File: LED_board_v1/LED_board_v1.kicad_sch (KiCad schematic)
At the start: 0 parts

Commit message: テープLED基板を作った(要修正+シルクメモ追加)
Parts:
- added C1, C13, C14, C15, C16, C19, C21, C4, C6, C8: 0.1uF, Capacitor_SMD:C_0603_1608Metric_Pad1.08x0.95mm_HandSolder, symbol Device:C_Small
- added C10, C12, C20, C9: 4.7μF, Capacitor_SMD:C_0805_2012Metric_Pad1.18x1.45mm_HandSolder, symbol Device:C
- added C11: 22μF, Capacitor_SMD:C_0805_2012Metric_Pad1.18x1.45mm_HandSolder, symbol Device:C
- added C17, C18: 4.7uF, Capacitor_SMD:C_0603_1608Metric_Pad1.08x0.95mm_HandSolder, symbol Device:C_Small
- added C5, C7: 100uF, Capacitor_THT:CP_Radial_D8.0mm_P3.50mm, symbol Device:C_Polarized
- added D2: D_Shockley, Diode_SMD:D_SOD-323_HandSoldering, symbol Device:D_Shockley
- added FB1: 120, Inductor_SMD:L_0603_1608Metric_Pad1.05x0.95mm_HandSolder, symbol Device:FerriteBead_Small
- added J1, J3: Conn_01x03_Pin, Connector_JST:JST_XH_S3B-XH-A_1x03_P2.50mm_Horizontal, symbol Connector:Conn_01x03_Pin
- added J12: Conn_01x02_Pin, Connector_AMASS:AMASS_XT30PW-M_1x02_P2.50mm_Horizontal, symbol Connector:Conn_01x02_Pin
- added J2: Conn_ST_STDC14, Connector_PinHeader_1.27mm:PinHeader_2x07_P1.27mm_Vertical, symbol Connector:Conn_ST_STDC14
- added R1: 10k, Resistor_SMD:R_0603_1608Metric_Pad0.98x0.95mm_HandSolder, symbol Device:R_Small
- added R2: 120, Resistor_SMD:R_0603_1608Metric_Pad0.98x0.95mm_HandSolder, symbol Device:R_Small
- added SW1: SW_Push, Button_Switch_THT:SW_PUSH_6mm, symbol Switch:SW_Push
- added SW2: SW_SPDT, Button_Switch_THT:SW_Slide-03_Wuerth-WS-SLTV_10x2.5x6.4_P2.54mm, symbol Switch:SW_SPDT
- added U1: PTCAN3414DDFR, 26off_tcan3414ddfr:SOT-23-THIN-8_DDF_TEX, symbol 26off_tcan3414ddfr:PTCAN3414DDFR
- added U2: STM32H533CETx, Package_QFP:LQFP-48_7x7mm_P0.5mm, symbol MCU_ST_STM32H5:STM32H533CETx
- added U3: NID60S48-24, Converter_DCDC:Converter_DCDC_MeanWell_NID60_THT, symbol Regulator_Switching:NID60S48-24
- added U4: BD33FC0FP, Package_TO_SOT_SMD:TO-252-2, symbol Regulator_Linear:BD33FC0FP
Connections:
- new net: FB1.1, U2.9 (VDDA)
- new net: C4.1, U3.11 (RC)
- new net: C18.1, U2.46 (VCAP)
- new net: R2.1, SW2.1 (A)
- new net: R1.1, U2.44 (BOOT0)
- new net: C17.1, U2.22 (VCAP)
- new net +24V: C5.1, C6.1, J12.2 (Pin_2), U3.7 (Vin), U3.8 (Vin)
- new net +3.3V: C1.2, C10.1, C11.1, C12.1, C13.1, C14.1, C15.1, C16.1, C20.2, C21.2, D2.2 (A), FB1.2, J2.3 (VCC), U1.3 (VCC), U2.1 (VBAT), U2.24 (VDD), U2.36 (VDD), U2.48 (VDD), U4.3 (VO)
- new net +5V: C7.1, C8.1, C9.1, D2.1 (K), U3.1 (Vout), U3.2 (Vout), U3.3 (Vout), U3.4 (Vout), U4.1 (VCC)
- new net GND: C1.1, C10.2, C11.2, C12.2, C13.2, C14.2, C15.2, C16.2, C17.2, C18.2, C19.2, C20.1, C21.1, C4.2, C5.2, C6.2, C7.2, C8.2, C9.2, J1.1 (Pin_1), J12.1 (Pin_1), J2.11 (GNDDetect), J2.5 (GND), J2.7 (GND), J3.3 (Pin_3), R1.2, SW1.1, U1.2 (GND), U1.5 (SHDN), U1.8 (STB), U2.23 (VSS), U2.35 (VSS), U2.47 (VSS), U2.8 (VSSA), U3.5 (COM), U3.6 (COM), U4.2 (GND)
- new net can_+: J1.3 (Pin_3), J3.1 (Pin_1), SW2.2 (B), U1.7 (CANH)
- new net can_-: J1.2 (Pin_2), J3.2 (Pin_2), R2.2, U1.6 (CANL)
- new net canrx: U1.4 (RXD), U2.32 (PA11)
- new net cantx: U1.1 (TXD), U2.33 (PA12)
- new net jtdi: J2.10 (JTDI/NC), U2.38 (PA15(JTDI))
- new net nrst: C19.1, J2.12 (~{RST}), SW1.2, U2.7 (NRST)
- new net strx: J2.13 (VCP_RX), U2.43 (PB7)
- new net sttx: J2.14 (VCP_TX), U2.42 (PB6)
- new net swclk: J2.6 (JCLK/SWCLK), U2.37 (PA14(JTCK)
- new net swdio: J2.4 (JTMS/SWDIO), U2.34 (PA13(JTMS)
- new net tapeled_1: U2.10 (PA0)
- new net tapeled_2: U2.11 (PA1)
- new net tapeled_3: U2.12 (PA2)
- new net tapeled_4: U2.13 (PA3)
- new net tapeled_5: U2.16 (PA6)
- new net tapeled_6: U2.17 (PA7)
- new net tapeled_7: U2.18 (PB0)
- new net tapeled_8: U2.19 (PB1)
- no-connect marks 0 -> 2
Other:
- added sheet logic_33to5_1 (74AHCT125 x4.kicad_sch)
- added sheet logic_33to5_2 (74AHCT125 x4.kicad_sch)
- note added: "3.3v変圧+逆流防止回路"
- note added: "High Low GND"
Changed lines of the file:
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@@
 	(generator_version "10.0")
 	(paper "A4")
-	(sheet_instances
-		(path "/"
-			(page "1")
-		)
-	)
-	(embedded_fonts no)
-)

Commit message: md改良(ちょっと前にしたやつ上げ忘れ)
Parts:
- added D1, D3: LED, LED_SMD:LED_0805_2012Metric_Pad1.15x1.40mm_HandSolder, symbol Device:LED
- added R3, R4: 1k, Resistor_SMD:R_0603_1608Metric_Pad0.98x0.95mm_HandSolder, symbol Device:R_Small
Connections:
- net GND: now also R3.2, R4.2
- net at U2.25 (PB12): now also D1.2 (A)
- net at U2.26 (PB13): now also D3.2 (A)
- new net: D3.1 (K), R4.1
- new net: D1.1 (K), R3.1

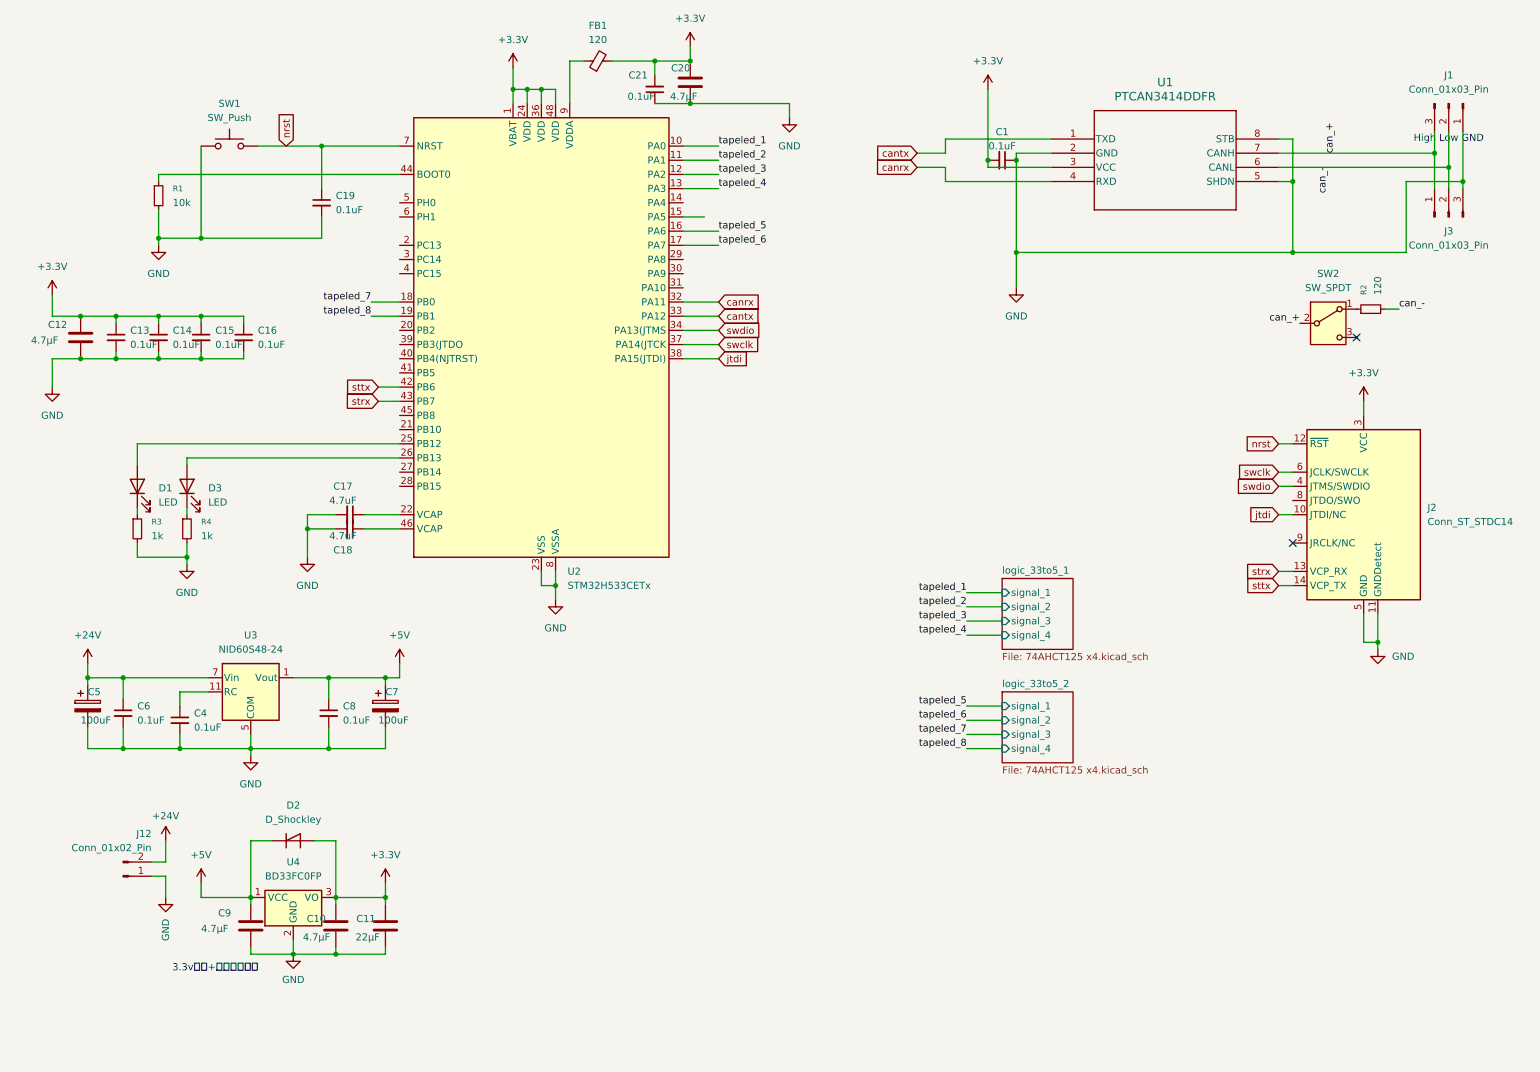
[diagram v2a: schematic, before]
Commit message: MDPID基板を作ったりLED基板の電源回りをいじった
MDPIDの電源変更+配線
LED基板の電源変更(未配線)
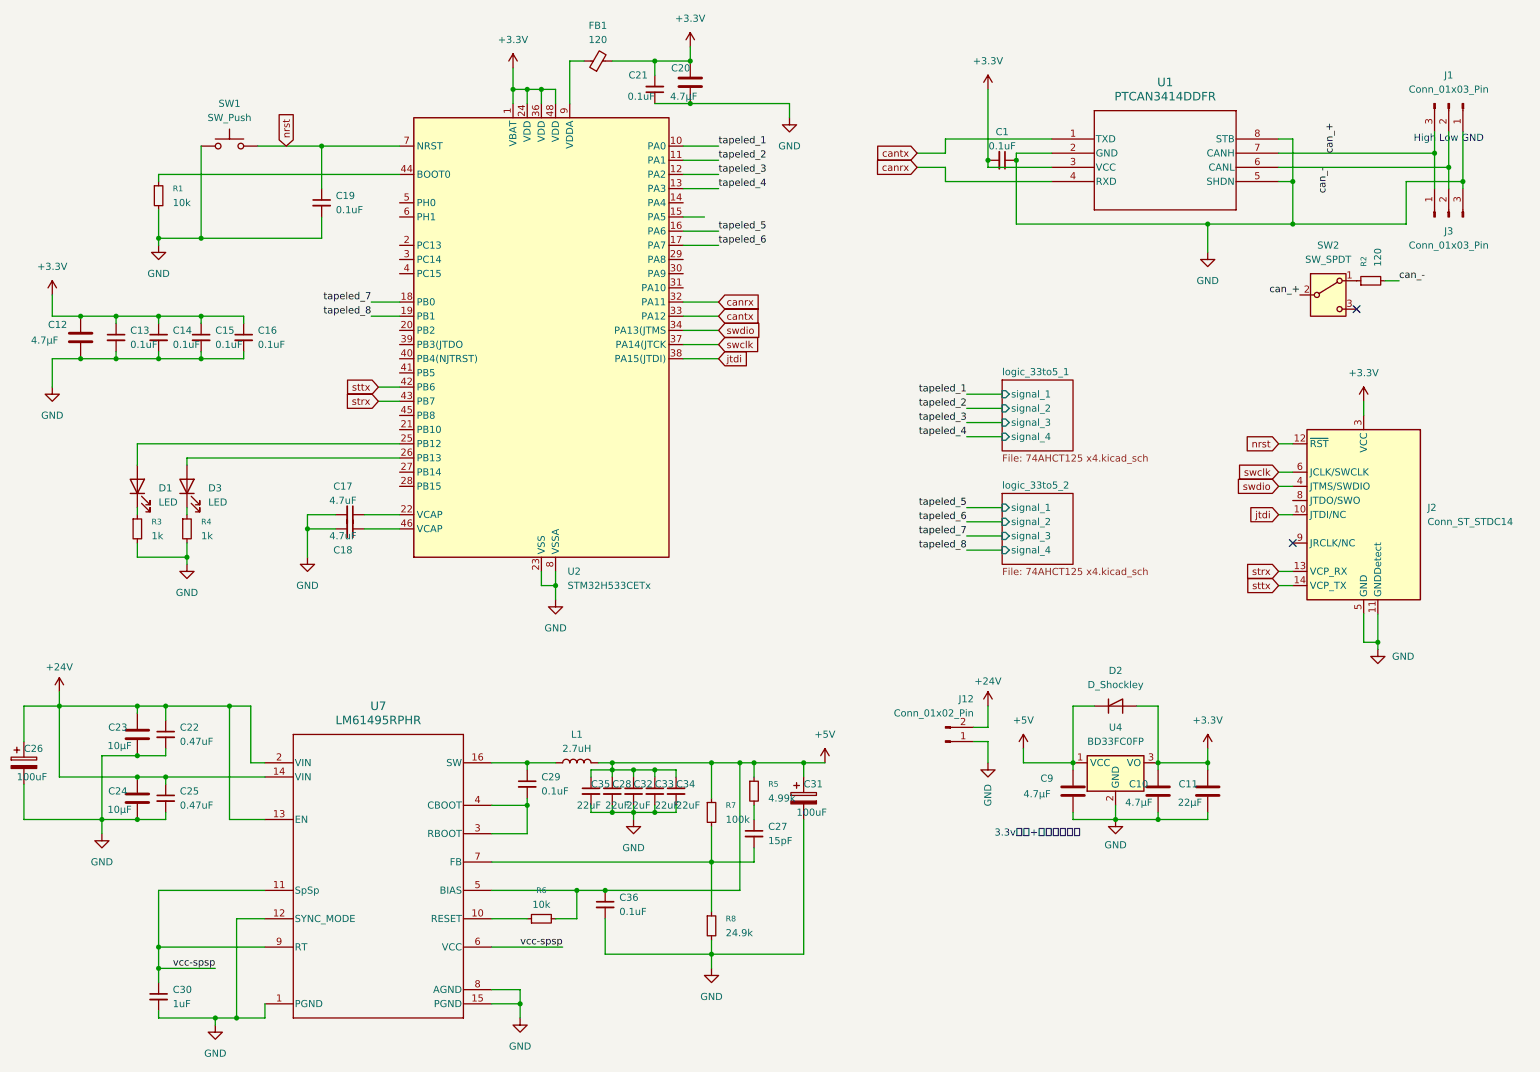
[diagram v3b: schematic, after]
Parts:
- removed C4, C6, C8: 0.1uF, Capacitor_SMD:C_0603_1608Metric_Pad1.08x0.95mm_HandSolder, symbol Device:C_Small
- removed C5, C7: 100uF, Capacitor_THT:CP_Radial_D8.0mm_P3.50mm, symbol Device:C_Polarized
- removed U3: NID60S48-24, Converter_DCDC:Converter_DCDC_MeanWell_NID60_THT, symbol Regulator_Switching:NID60S48-24
- added C22, C25: 0.47uF, Capacitor_SMD:C_0603_1608Metric_Pad1.08x0.95mm_HandSolder, symbol Device:C_Small
- added C23, C24: 10μF, Capacitor_SMD:C_0805_2012Metric_Pad1.18x1.45mm_HandSolder, symbol Device:C
- added C26, C31: 100uF, Capacitor_THT:CP_Radial_D8.0mm_P3.50mm, symbol Device:C_Polarized
- added C27: 15pF, Capacitor_SMD:C_0603_1608Metric_Pad1.08x0.95mm_HandSolder, symbol Device:C_Small
- added C28, C32, C33, C34, C35: 22uF, Capacitor_SMD:C_0603_1608Metric_Pad1.08x0.95mm_HandSolder, symbol Device:C_Small
- added C29, C36: 0.1uF, Capacitor_SMD:C_0603_1608Metric_Pad1.08x0.95mm_HandSolder, symbol Device:C_Small
- added C30: 1uF, Capacitor_SMD:C_0603_1608Metric_Pad1.08x0.95mm_HandSolder, symbol Device:C_Small
- added L1: 2.7uH, Inductor_SMD:L_APV_APH1250, symbol Device:L
- added R5: 4.99k, Resistor_SMD:R_0603_1608Metric_Pad0.98x0.95mm_HandSolder, symbol Device:R_Small
- added R6: 10k, Resistor_SMD:R_0603_1608Metric_Pad0.98x0.95mm_HandSolder, symbol Device:R_Small
- added R7: 100k, Resistor_SMD:R_0603_1608Metric_Pad0.98x0.95mm_HandSolder, symbol Device:R_Small
- added R8: 24.9k, Resistor_SMD:R_0603_1608Metric_Pad0.98x0.95mm_HandSolder, symbol Device:R_Small
- added U7: LM61495RPHR, LM61495:RPH0016A, symbol 26off_LM61495:LM61495RPHR
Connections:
- net +24V: now also C22.1, C23.1, C24.1, C25.1, C26.1, U7.13 (EN), U7.14 (VIN), U7.2 (VIN)
- net +5V: now also C28.1, C31.1, C32.1, C33.1, C34.1, C35.1, C36.1, L1.2, R5.1, R6.2, R7.1, U7.5 (BIAS)
- net GND: now also C22.2, C23.2, C24.2, C25.2, C26.2, C28.2, C30.2, C31.2, C32.2, C33.2, C34.2, C35.2, C36.2, R8.2, U7.1 (PGND), U7.12 (SYNC_MODE), U7.15 (PGND), U7.8 (AGND)
- new net: C27.1, R5.2
- new net: R6.1, U7.10 (RESET)
- new net: C27.2, R7.2, R8.1, U7.7 (FB)
- new net: C29.1, L1.1, U7.16 (SW)
- new net: C29.2, U7.3 (RBOOT), U7.4 (CBOOT)
- new net vcc-spsp: C30.1, U7.11 (SpSp), U7.6 (VCC), U7.9 (RT)
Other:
- moved on the sheet: C10, C11, C9, D2, J12, R2, SW2, U4
